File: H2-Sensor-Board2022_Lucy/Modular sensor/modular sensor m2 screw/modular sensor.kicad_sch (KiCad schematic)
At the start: 4 parts, among them J1 Conn_01x03_Pin, U1 MQ-8

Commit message: Small revision🐱‍💻
Actually made it properly 🐱‍💻
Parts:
- R1: footprint Resistor_SMD:R_0402_1005Metric_Pad0.72x0.64mm_HandSolder -> Resistor_SMD:R_0805_2012Metric_Pad1.20x1.40mm_HandSolder
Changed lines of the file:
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@@
       (effects (font (size 1.27 1.27)) (justify left))
     )
-    (property "Footprint" "Resistor_SMD:R_0402_1005Metric_Pad0.72x0.64mm_HandSolder" (at 130.556 91.694 90)
+    (property "Footprint" "Resistor_SMD:R_0805_2012Metric_Pad1.20x1.40mm_HandSolder" (at 130.556 91.694 90)
       (effects (font (size 1.27 1.27)) hide)
     )

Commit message: ups
oops
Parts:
- C1: footprint Capacitor_SMD:C_0402_1005Metric -> Capacitor_SMD:C_1206_3216Metric_Pad1.33x1.80mm_HandSolder
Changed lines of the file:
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@@
       (effects (font (size 1.27 1.27)) (justify left))
     )
-    (property "Footprint" "Capacitor_SMD:C_0402_1005Metric" (at 160.02 97.79 0)
+    (property "Footprint" "Capacitor_SMD:C_1206_3216Metric_Pad1.33x1.80mm_HandSolder" (at 160.02 97.79 0)
       (effects (font (size 1.27 1.27)) hide)
     )

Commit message: 👆
update
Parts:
- added H1: MountingHole_Pad, MountingHole:MountingHole_2.7mm_M2.5_Pad_Via, symbol Mechanical:MountingHole_Pad
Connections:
- net GND: now also H1.1
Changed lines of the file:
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@@
   (junction (at 160.02 100.33) (diameter 0) (color 0 0 0 0)
   )
+  (junction (at 154.94 100.33) (diameter 0) (color 0 0 0 0)
+  )
   (junction (at 129.54 100.33) (diameter 0) (color 0 0 0 0)
   )
@@
   )
   (wire (pts (xy 160.02 100.33) (xy 167.64 100.33))
+    (stroke (width 0) (type default))
+  )
+  (wire (pts (xy 154.94 100.33) (xy 154.94 105.41))
     (stroke (width 0) (type default))
   )
@@
         )
       )
+    )
+  )
+  (symbol (lib_id "Mechanical:MountingHole_Pad") (at 154.94 107.95 180) (unit 1)
+    (in_bom yes) (on_board yes) (dnp no) (fields_autoplaced)
+    (property "Reference" "H1" (at 157.48 107.95 0)
+      (effects (font (size 1.27 1.27)) (justify right))
+    )
+    (property "Value" "MountingHole_Pad" (at 157.48 110.49 0)
+      (effects (font (size 1.27 1.27)) (justify right))
+    )
+    (property "Footprint" "MountingHole:MountingHole_2.7mm_M2.5_Pad_Via" (at 154.94 107.95 0)
+      (effects (font (size 1.27 1.27)) hide)
+    )
+    (property "Datasheet" "~" (at 154.94 107.95 0)
+      (effects (font (size 1.27 1.27)) hide)
+    )
+    (pin "1")
+    (instances
+      (project "modular sensor"
+        (path "/ab6f5795-0bed-45ee-8b18-fd9bd5bfbe26"
+          (reference "H1") (unit 1)
+        )
+      )

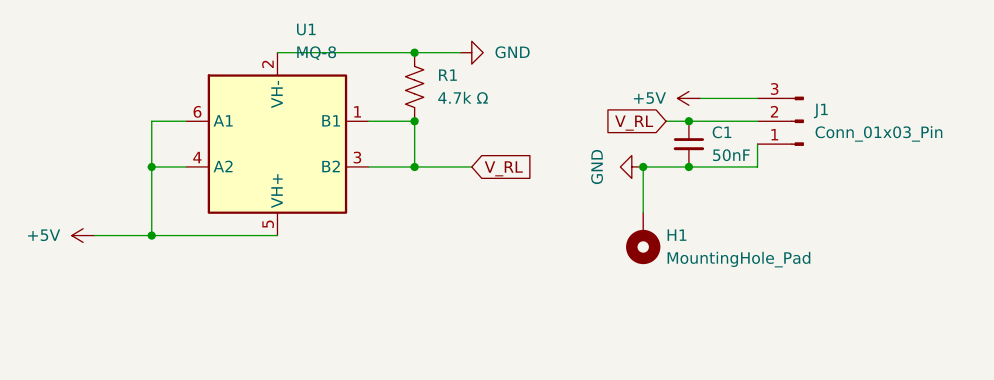
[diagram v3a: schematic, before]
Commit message: MQ-8 holes slightly larger
mq-8 de-soldering hopefully won't be a pain?
silk screen added
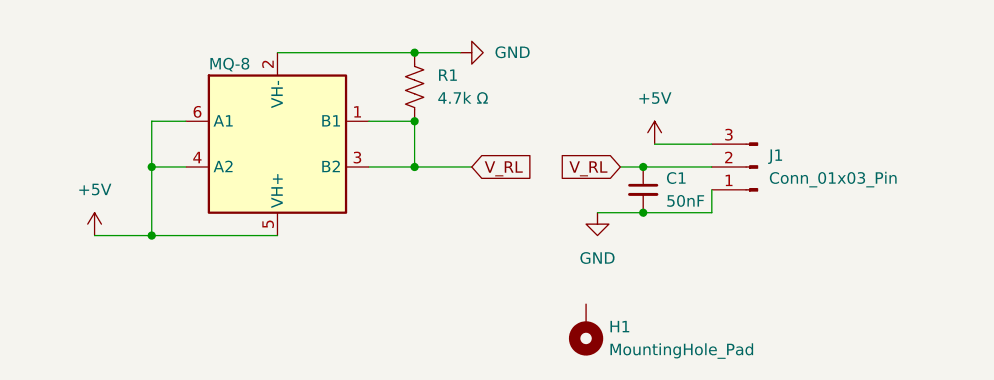
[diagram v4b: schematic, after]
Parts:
- R1: footprint Resistor_SMD:R_0805_2012Metric_Pad1.20x1.40mm_HandSolder -> Resistor_SMD:R_1206_3216Metric_Pad1.30x1.75mm_HandSolder
- renumbered U1 to MQ-8
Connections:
- net GND: no longer H1.1
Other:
- moved on the sheet: C1, H1, J1
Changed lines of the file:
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@@
   (junction (at 129.54 95.25) (diameter 0) (color 0 0 0 0)
   )
-  (junction (at 160.02 95.25) (diameter 0) (color 0 0 0 0)
+  (junction (at 154.94 100.33) (diameter 0) (color 0 0 0 0)
   )
   (junction (at 100.33 107.95) (diameter 0) (color 0 0 0 0)
   )
-  (junction (at 160.02 100.33) (diameter 0) (color 0 0 0 0)
-  )
-  (junction (at 154.94 100.33) (diameter 0) (color 0 0 0 0)
+  (junction (at 154.94 105.41) (diameter 0) (color 0 0 0 0)
   )
   (junction (at 129.54 100.33) (diameter 0) (color 0 0 0 0)
@@
     (stroke (width 0) (type default))
   )
-  (wire (pts (xy 161.29 92.71) (xy 167.64 92.71))
+  (wire (pts (xy 156.21 97.79) (xy 162.56 97.79))
     (stroke (width 0) (type default))
   )
@@
     (stroke (width 0) (type default))
   )
-  (wire (pts (xy 160.02 100.33) (xy 167.64 100.33))
-    (stroke (width 0) (type default))
-  )
-  (wire (pts (xy 154.94 100.33) (xy 154.94 105.41))
+  (wire (pts (xy 154.94 105.41) (xy 162.56 105.41))
     (stroke (width 0) (type default))
   )
@@
     (stroke (width 0) (type default))
   )
-  (wire (pts (xy 167.64 100.33) (xy 167.64 97.79))
-    (stroke (width 0) (type default))
-  )
-  (wire (pts (xy 157.48 95.25) (xy 160.02 95.25))
-    (stroke (width 0) (type default))
-  )
-  (wire (pts (xy 160.02 95.25) (xy 167.64 95.25))
-    (stroke (width 0) (type default))
-  )
-  (wire (pts (xy 154.94 100.33) (xy 160.02 100.33))
+  (wire (pts (xy 162.56 105.41) (xy 162.56 102.87))
+    (stroke (width 0) (type default))
+  )
+  (wire (pts (xy 152.4 100.33) (xy 154.94 100.33))
+    (stroke (width 0) (type default))
+  )
+  (wire (pts (xy 154.94 100.33) (xy 162.56 100.33))
+    (stroke (width 0) (type default))
+  )
+  (wire (pts (xy 149.86 105.41) (xy 154.94 105.41))
     (stroke (width 0) (type default))
   )
@@
     (stroke (width 0) (type default))
   )
-  (global_label "V_RL" (shape input) (at 157.48 95.25 180) (fields_autoplaced)
+  (global_label "V_RL" (shape input) (at 152.4 100.33 180) (fields_autoplaced)
     (effects (font (size 1.27 1.27)) (justify right))
-    (property "Intersheetrefs" "${INTERSHEET_REFS}" (at 150.1405 95.25 0)
+    (property "Intersheetrefs" "${INTERSHEET_REFS}" (at 145.0605 100.33 0)
       (effects (font (size 1.27 1.27)) (justify right) hide)
     )
@@
   )
   (symbol (lib_id "Sensor_h2sen_winsen_mq8:MQ-8") (at 114.3 97.79 0) (unit 1)
-    (in_bom yes) (on_board yes) (dnp no) (fields_autoplaced)
-    (property "Reference" "U1" (at 116.3194 85.09 0)
+    (in_bom yes) (on_board yes) (dnp no)
+    (property "Reference" "MQ-8" (at 106.68 88.9 0)
       (effects (font (size 1.27 1.27)) (justify left))
     )
     (property "Value" "MQ-8" (at 116.3194 87.63 0)
-      (effects (font (size 1.27 1.27)) (justify left))
+      (effects (font (size 1.27 1.27)) (justify left) hide)
     )
     (property "Footprint" "Modular sensor footprints:MQ-8" (at 86.36 114.3 0)
@@
       (project "modular sensor"
         (path "/ab6f5795-0bed-45ee-8b18-fd9bd5bfbe26"
-          (reference "U1") (unit 1)
-        )
-      )
-    )
-  )
-  (symbol (lib_id "power:+5V") (at 161.29 92.71 90) (unit 1)
-    (in_bom yes) (on_board yes) (dnp no) (fields_autoplaced)
-    (property "Reference" "#PWR02" (at 165.1 92.71 0)
-      (effects (font (size 1.27 1.27)) hide)
-    )
-    (property "Value" "+5V" (at 157.48 92.7099 90)
-      (effects (font (size 1.27 1.27)) (justify left))
-    )
-    (property "Footprint" "" (at 161.29 92.71 0)
-      (effects (font (size 1.27 1.27)) hide)
-    )
-    (property "Datasheet" "" (at 161.29 92.71 0)
+          (reference "MQ-8") (unit 1)
+        )
+      )
+    )
+  )
+  (symbol (lib_id "power:+5V") (at 156.21 97.79 0) (unit 1)
+    (in_bom yes) (on_board yes) (dnp no) (fields_autoplaced)
+    (property "Reference" "#PWR02" (at 156.21 101.6 0)
+      (effects (font (size 1.27 1.27)) hide)
+    )
+    (property "Value" "+5V" (at 156.21 92.71 0)
+      (effects (font (size 1.27 1.27)))
+    )
+    (property "Footprint" "" (at 156.21 97.79 0)
+      (effects (font (size 1.27 1.27)) hide)
+    )
+    (property "Datasheet" "" (at 156.21 97.79 0)
       (effects (font (size 1.27 1.27)) hide)
     )
@@
       (effects (font (size 1.27 1.27)) (justify left))
     )
-    (property "Footprint" "Resistor_SMD:R_0805_2012Metric_Pad1.20x1.40mm_HandSolder" (at 130.556 91.694 90)
+    (property "Footprint" "Resistor_SMD:R_1206_3216Metric_Pad1.30x1.75mm_HandSolder" (at 130.556 91.694 90)
       (effects (font (size 1.27 1.27)) hide)
     )
@@
     )
   )
-  (symbol (lib_id "Connector:Conn_01x03_Pin") (at 172.72 95.25 180) (unit 1)
-    (in_bom yes) (on_board yes) (dnp no) (fields_autoplaced)
-    (property "Reference" "J1" (at 173.99 93.98 0)
-      (effects (font (size 1.27 1.27)) (justify right))
-    )
-    (property "Value" "Conn_01x03_Pin" (at 173.99 96.52 0)
-      (effects (font (size 1.27 1.27)) (justify right))
-    )
-    (property "Footprint" "Connector_PinHeader_2.54mm:PinHeader_1x03_P2.54mm_Vertical" (at 172.72 95.25 0)
-      (effects (font (size 1.27 1.27)) hide)
-    )
-    (property "Datasheet" "~" (at 172.72 95.25 0)
+  (symbol (lib_id "Connector:Conn_01x03_Pin") (at 167.64 100.33 180) (unit 1)
+    (in_bom yes) (on_board yes) (dnp no) (fields_autoplaced)
+    (property "Reference" "J1" (at 168.91 99.06 0)
+      (effects (font (size 1.27 1.27)) (justify right))
+    )
+    (property "Value" "Conn_01x03_Pin" (at 168.91 101.6 0)
+      (effects (font (size 1.27 1.27)) (justify right))
+    )
+    (property "Footprint" "Connector_PinHeader_2.54mm:PinHeader_1x03_P2.54mm_Vertical" (at 167.64 100.33 0)
+      (effects (font (size 1.27 1.27)) hide)
+    )
+    (property "Datasheet" "~" (at 167.64 100.33 0)
       (effects (font (size 1.27 1.27)) hide)
     )
@@
     )
   )
-  (symbol (lib_id "Mechanical:MountingHole_Pad") (at 154.94 107.95 180) (unit 1)
-    (in_bom yes) (on_board yes) (dnp no) (fields_autoplaced)
-    (property "Reference" "H1" (at 157.48 107.95 0)
-      (effects (font (size 1.27 1.27)) (justify right))
-    )
-    (property "Value" "MountingHole_Pad" (at 157.48 110.49 0)
-      (effects (font (size 1.27 1.27)) (justify right))
-    )
-    (property "Footprint" "MountingHole:MountingHole_2.7mm_M2.5_Pad_Via" (at 154.94 107.95 0)
-      (effects (font (size 1.27 1.27)) hide)
-    )
-    (property "Datasheet" "~" (at 154.94 107.95 0)
+  (symbol (lib_id "Mechanical:MountingHole_Pad") (at 148.59 118.11 180) (unit 1)
+    (in_bom yes) (on_board yes) (dnp no) (fields_autoplaced)
+    (property "Reference" "H1" (at 151.13 118.11 0)
+      (effects (font (size 1.27 1.27)) (justify right))
+    )
+    (property "Value" "MountingHole_Pad" (at 151.13 120.65 0)
+      (effects (font (size 1.27 1.27)) (justify right))
+    )
+    (property "Footprint" "MountingHole:MountingHole_2.7mm_M2.5_Pad_Via" (at 148.59 118.11 0)
+      (effects (font (size 1.27 1.27)) hide)
+    )
+    (property "Datasheet" "~" (at 148.59 118.11 0)
       (effects (font (size 1.27 1.27)) hide)
     )
@@
     )
   )
-  (symbol (lib_id "power:GND") (at 154.94 100.33 270) (unit 1)
-    (in_bom yes) (on_board yes) (dnp no) (fields_autoplaced)
-    (property "Reference" "#PWR01" (at 148.59 100.33 0)
-      (effects (font (size 1.27 1.27)) hide)
-    )
-    (property "Value" "GND" (at 149.86 100.33 0)
+  (symbol (lib_id "power:GND") (at 149.86 105.41 0) (unit 1)
+    (in_bom yes) (on_board yes) (dnp no) (fields_autoplaced)
+    (property "Reference" "#PWR01" (at 149.86 111.76 0)
+      (effects (font (size 1.27 1.27)) hide)
+    )
+    (property "Value" "GND" (at 149.86 110.49 0)
       (effects (font (size 1.27 1.27)))
     )
-    (property "Footprint" "" (at 154.94 100.33 0)
-      (effects (font (size 1.27 1.27)) hide)
-    )
-    (property "Datasheet" "" (at 154.94 100.33 0)
+    (property "Footprint" "" (at 149.86 105.41 0)
+      (effects (font (size 1.27 1.27)) hide)
+    )
+    (property "Datasheet" "" (at 149.86 105.41 0)
       (effects (font (size 1.27 1.27)) hide)
     )
@@
     )
   )
-  (symbol (lib_id "power:+5V") (at 93.98 107.95 90) (unit 1)
-    (in_bom yes) (on_board yes) (dnp no) (fields_autoplaced)
-    (property "Reference" "#PWR0101" (at 97.79 107.95 0)
-      (effects (font (size 1.27 1.27)) hide)
-    )
-    (property "Value" "+5V" (at 90.17 107.9499 90)
-      (effects (font (size 1.27 1.27)) (justify left))
+  (symbol (lib_id "power:+5V") (at 93.98 107.95 0) (unit 1)
+    (in_bom yes) (on_board yes) (dnp no) (fields_autoplaced)
+    (property "Reference" "#PWR0101" (at 93.98 111.76 0)
+      (effects (font (size 1.27 1.27)) hide)
+    )
+    (property "Value" "+5V" (at 93.98 102.87 0)
+      (effects (font (size 1.27 1.27)))
     )
     (property "Footprint" "" (at 93.98 107.95 0)
@@
     )
   )
-  (symbol (lib_id "Device:C_Small") (at 160.02 97.79 0) (unit 1)
-    (in_bom yes) (on_board yes) (dnp no) (fields_autoplaced)
-    (property "Reference" "C1" (at 162.56 96.5263 0)
-      (effects (font (size 1.27 1.27)) (justify left))
-    )
-    (property "Value" "50nF" (at 162.56 99.0663 0)
-      (effects (font (size 1.27 1.27)) (justify left))
-    )
-    (property "Footprint" "Capacitor_SMD:C_1206_3216Metric_Pad1.33x1.80mm_HandSolder" (at 160.02 97.79 0)
-      (effects (font (size 1.27 1.27)) hide)
-    )
-    (property "Datasheet" "~" (at 160.02 97.79 0)
-      (effects (font (size 1.27 1.27)) hide)
-    )
+  (symbol (lib_id "Device:C_Small") (at 154.94 102.87 0) (unit 1)
+    (in_bom yes) (on_board yes) (dnp no) (fields_autoplaced)
+    (property "Reference" "C1" (at 157.48 101.6063 0)
+      (effects (font (size 1.27 1.27)) (justify left))
+    )
+    (property "Value" "50nF" (at 157.48 104.1463 0)
+      (effects (font (size 1.27 1.27)) (justify left))
+    )
+    (property "Footprint" "Capacitor_SMD:C_1206_3216Metric_Pad1.33x1.80mm_HandSolder" (at 154.94 102.87 0)
+      (effects (font (size 1.27 1.27)) hide)
+    )
+    (property "Datasheet" "~" (at 154.94 102.87 0)
+      (effects (font (size 1.27 1.27)) hide)
+    )

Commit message: should be jlc ready
should be within jlc specs
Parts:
- C1: LCSC (none) -> C9807
- J1: LCSC (none) -> C49257
- R1: LCSC (none) -> C414910
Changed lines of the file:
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@@
+      (effects (font (size 1.27 1.27)) hide)
+    )
+    (property "LCSC" "C414910" (at 129.54 91.44 0)
       (effects (font (size 1.27 1.27)) hide)
     )
@@
     )
     (property "Datasheet" "~" (at 167.64 100.33 0)
+      (effects (font (size 1.27 1.27)) hide)
+    )
+    (property "LCSC" "C49257" (at 167.64 100.33 0)
       (effects (font (size 1.27 1.27)) hide)
     )
@@
       (effects (font (size 1.27 1.27)) hide)
     )
+    (property "LCSC" "C9807" (at 154.94 102.87 0)
+      (effects (font (size 1.27 1.27)) hide)
+    )
